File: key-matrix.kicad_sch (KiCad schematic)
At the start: 210 parts, among them SW1 esc, SW10 f9, SW100 R ctrl, SW101 Left, SW102 down, SW103 right, SW104 num zero, SW105 num full stop, SW11 f10, SW12 f11, SW13 f12, SW14 prtscr, SW15 scrlck, SW16 pause, SW17 tilde, SW18 1, SW19 2, SW2 f1, SW20 3, SW21 4, SW22 5, SW23 6, SW24 7, SW25 8, SW26 9, SW27 0, SW28 minus, SW29 equals, SW3 f2, SW30 backspace, SW31 insert, SW32 home, SW33 pgup, SW34 num lock, SW35 num slash, SW36 num mult, SW37 num minus, SW38 tab, SW39 q, SW4 f3, SW40 w, SW41 e, SW42 r, SW43 t, SW44 y, SW45 u, SW46 i, SW47 o, SW48 p, SW49 L brac, SW5 f4, SW50 R brac, SW51 enter, SW52 delete, SW53 end, SW54 pgdn, SW55 num 7, SW56 num 8, SW57 num 9, SW58 num add, SW59 capslock, SW6 f5, SW60 a, SW61 s, SW62 d, SW63 f, SW64 g, SW65 h, SW66 j, SW67 k, SW68 l, SW69 sem colon, SW7 f6, SW70 quote, SW71 tilde, SW72 num 4, SW73 num 5, SW74 num 6, SW75 L shift, SW76 backslash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

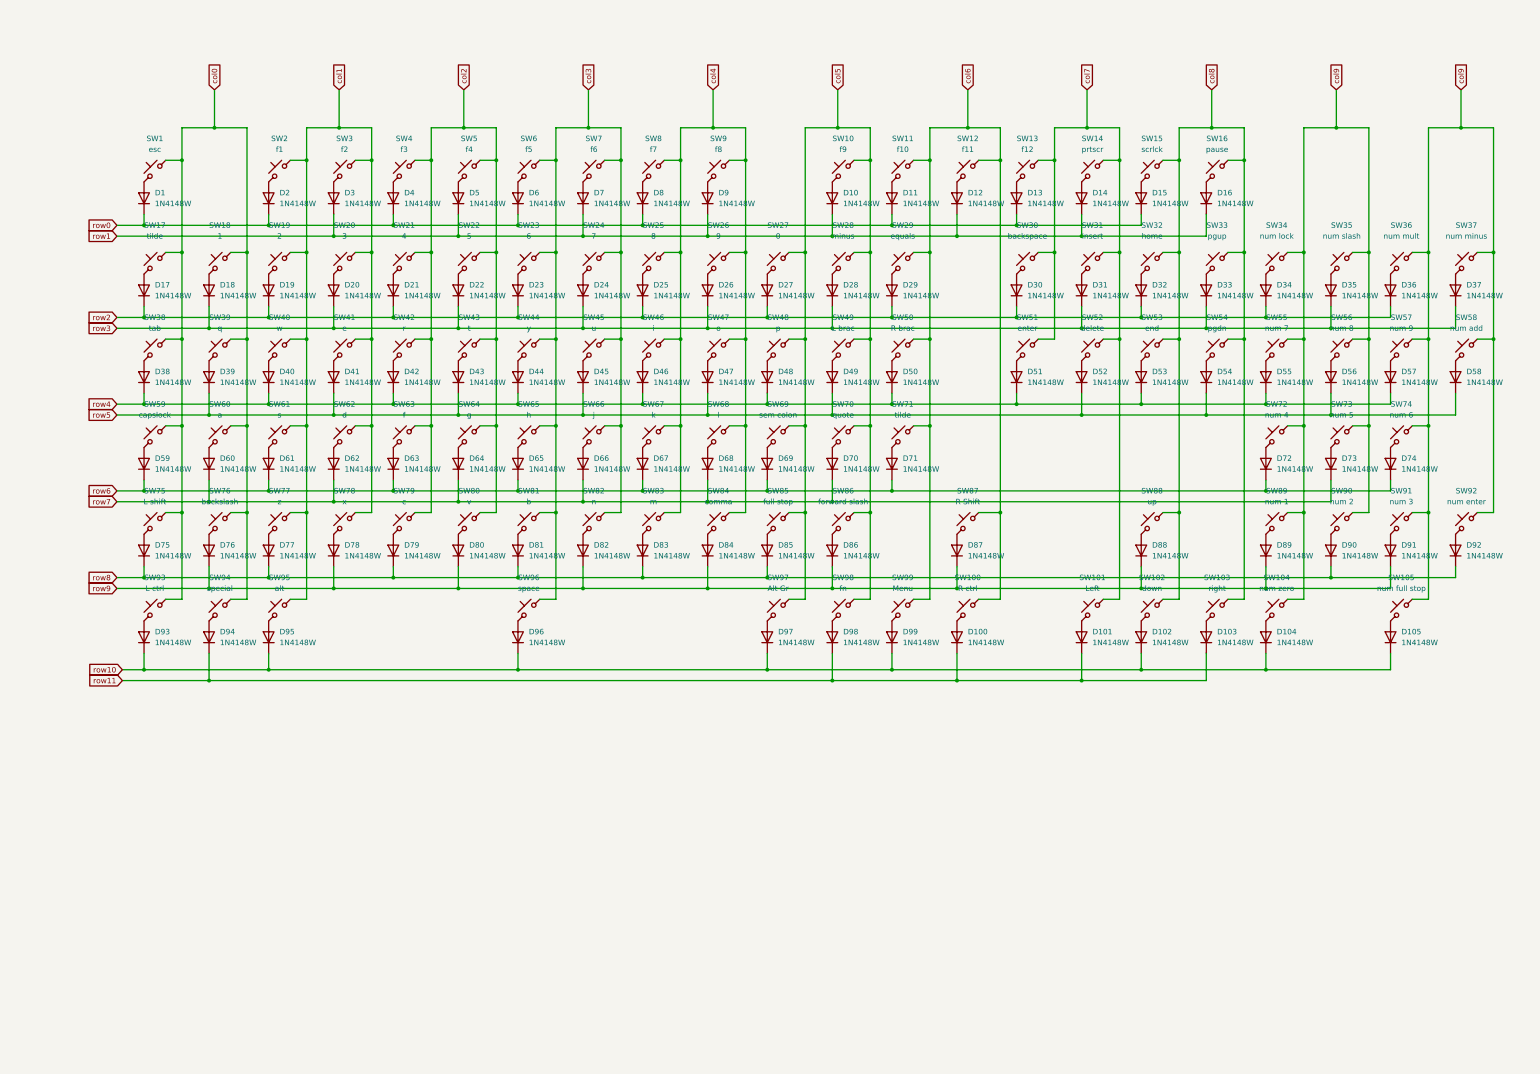
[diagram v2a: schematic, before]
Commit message: Started keyboard matrix, completed all rows, completed numpad columns
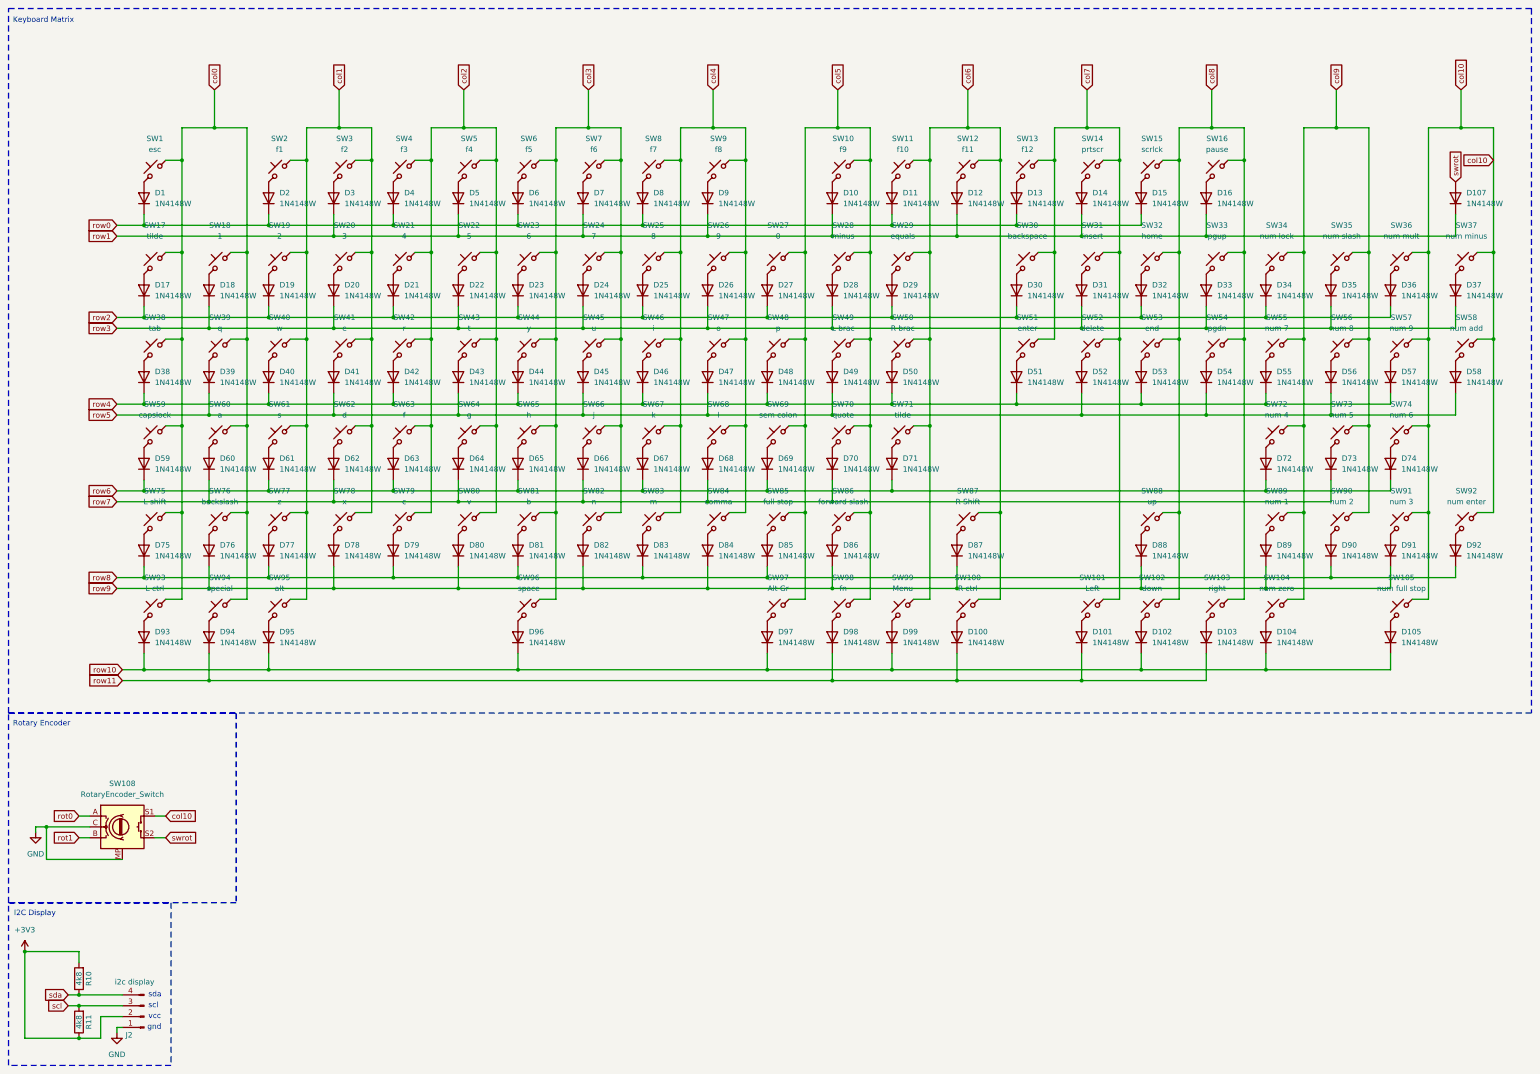
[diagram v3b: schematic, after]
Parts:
- added D107: 1N4148W, Diode_SMD:D_SOD-123, symbol Diode:1N4148WT
- added J2: i2c display, jacob-libs:0.91 OLED I2C DISPLAY, symbol Connector:Conn_01x04_Pin
- added R10, R11: 4k8, Resistor_SMD:R_0805_2012Metric_Pad1.20x1.40mm_HandSolder, symbol Device:R
- added SW108: RotaryEncoder_Switch, Rotary_Encoder:RotaryEncoder_Alps_EC11E-Switch_Vertical_H20mm, symbol Device:RotaryEncoder_Switch_MP
- SW100, SW93, SW94, SW95, SW97, SW98, SW99: footprint Gateron_KS33_Hotswap:Gateron-KS33-Hotswap-1U -> Gateron_KS33_Hotswap:Gateron-KS33-Hotswap-1.25U
- SW104: footprint Gateron_KS33_Hotswap:Gateron-KS33-Hotswap-1U -> Gateron_KS33_Hotswap:Gateron-KS33-Hotswap-2U
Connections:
- net col9: no longer SW105.1, SW36.1, SW37.1, SW57.1, SW58.1, SW74.1, SW91.1, SW92.1
- net row1: now also D107.1 (K)
- new net +3V3: J2.2 (Pin_2), R10.2, R11.1
- new net GND: J2.1 (Pin_1), SW108.C, SW108.MP
- new net col10: SW105.1, SW108.S1, SW36.1, SW37.1, SW57.1, SW58.1, SW74.1, SW91.1, SW92.1
- new net rot0: SW108.A
- new net rot1: SW108.B
- new net scl: J2.3 (Pin_3), R11.2
- new net sda: J2.4 (Pin_4), R10.1
- new net swrot: D107.2 (A), SW108.S2
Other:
- note added: "I2C Display"
- note added: "Keyboard Matrix"
- note added: "Rotary Encoder"
- note added: "gnd"
- note added: "scl"
- note added: "sda"
- note added: "vcc"
